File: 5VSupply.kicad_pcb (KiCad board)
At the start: 2 copper layers, 20.2 x 13 mm, 15 parts, among them J1 Conn_01x02, J2 Conn_01x02, U1 TPS560200DBVR

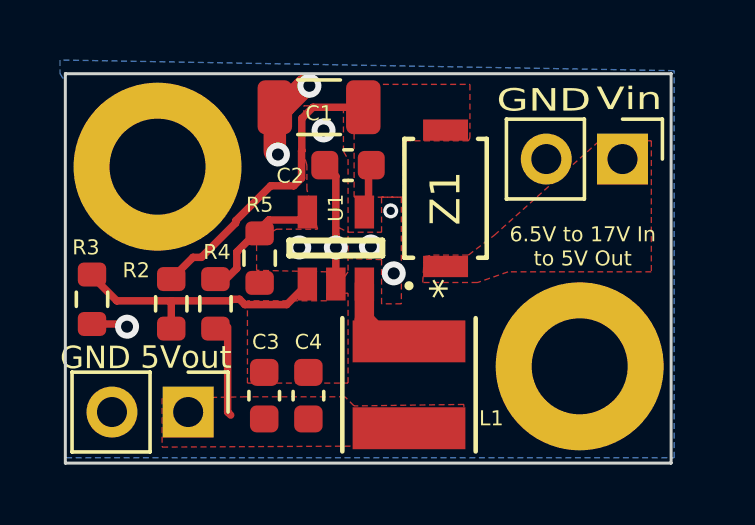
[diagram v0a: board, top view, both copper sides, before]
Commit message: PCB submitted for order
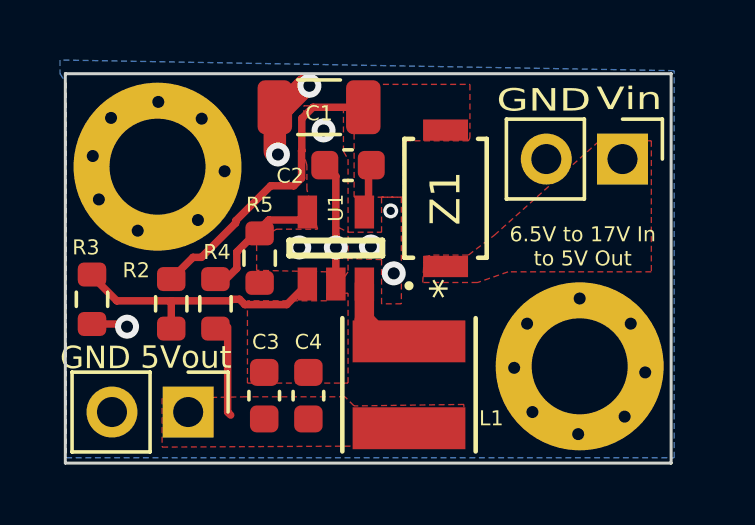
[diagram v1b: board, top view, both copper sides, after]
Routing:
- net GND: vias 9 -> 25
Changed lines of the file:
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@@
     (fp_arc (start -0.724999 1.475) (mid -0.778213 1.452901) (end -0.80074 1.399867)
       (stroke (width 0.127) (type solid)) (layer "F.Fab"))
-    (fp_arc (start 0.723714 -1.445998) (mid 0.776937 -1.423889) (end 0.799455 -1.37084)
+    (fp_arc (start 0.723714 -1.445998) (mid 0.77694 -1.423891) (end 0.799455 -1.37084)
       (stroke (width 0.127) (type solid)) (layer "F.Fab"))
-    (fp_arc (start 0.799455 1.399868) (mid 0.776925 1.452897) (end 0.723713 1.475)
+    (fp_arc (start 0.799455 1.399868) (mid 0.776922 1.452894) (end 0.723713 1.475)
       (stroke (width 0.127) (type solid)) (layer "F.Fab"))
     (pad "1" smd rect (at -1.2 -0.950001 180) (size 0.650001 1.1) (layers "F.Cu" "F.Paste" "F.Mask")
@@
   (segment (start 136.5118 80.073) (end 136.6012 80.1624) (width 0.25) (layer "F.Cu") (net 2))
   (segment (start 143.0906 74.8792) (end 143.1922 74.7776) (width 0.25) (layer "F.Cu") (net 2))
+  (via (at 149.5044 81.534) (size 0.8) (drill 0.4) (layers "F.Cu" "B.Cu") (net 2))
+  (via (at 153.8732 81.6864) (size 0.8) (drill 0.4) (layers "F.Cu" "B.Cu") (net 2))
   (via (at 136.6012 80.1624) (size 0.8) (drill 0.4) (layers "F.Cu" "B.Cu") (net 2))
+  (via (at 151.638 83.7438) (size 0.8) (drill 0.4) (layers "F.Cu" "B.Cu") (net 2))
+  (via (at 150.114 83.0072) (size 0.8) (drill 0.4) (layers "F.Cu" "B.Cu") (net 2))
+  (via (at 136.9568 76.962) (size 0.8) (drill 0.4) (layers "F.Cu" "B.Cu") (net 2))
   (via (at 145.3896 76.3016) (size 0.5) (drill 0.275) (layers "F.Cu" "B.Cu") (net 2))
   (via (at 142.679693 72.132557) (size 0.8) (drill 0.4) (layers "F.Cu" "B.Cu") (net 2))
+  (via (at 139.8524 74.9808) (size 0.8) (drill 0.4) (layers "F.Cu" "B.Cu") (net 2))
+  (via (at 139.0904 73.2282) (size 0.8) (drill 0.4) (layers "F.Cu" "B.Cu") (net 2))
+  (via (at 137.6426 72.6694) (size 0.8) (drill 0.4) (layers "F.Cu" "B.Cu") (net 2))
+  (via (at 153.3906 80.0608) (size 0.8) (drill 0.4) (layers "F.Cu" "B.Cu") (net 2))
   (via (at 142.3416 77.5208) (size 0.8) (drill 0.4) (layers "F.Cu" "B.Cu") (net 2))
   (via (at 144.7292 77.489502) (size 0.8) (drill 0.4) (layers "F.Cu" "B.Cu") (net 2))
   (via (at 141.6304 74.422) (size 0.8) (drill 0.4) (layers "F.Cu" "B.Cu") (net 2))
+  (via (at 151.6888 79.2226) (size 0.8) (drill 0.4) (layers "F.Cu" "B.Cu") (net 2))
+  (via (at 138.9634 76.6064) (size 0.8) (drill 0.4) (layers "F.Cu" "B.Cu") (net 2))
   (via (at 145.4912 78.3844) (size 0.8) (drill 0.4) (layers "F.Cu" "B.Cu") (net 2))
+  (via (at 136.0678 73.2028) (size 0.8) (drill 0.4) (layers "F.Cu" "B.Cu") (net 2))
+  (via (at 149.9362 80.0608) (size 0.8) (drill 0.4) (layers "F.Cu" "B.Cu") (net 2))
+  (via (at 135.6614 75.9206) (size 0.8) (drill 0.4) (layers "F.Cu" "B.Cu") (net 2))
+  (via (at 153.1874 83.1596) (size 0.8) (drill 0.4) (layers "F.Cu" "B.Cu") (net 2))
   (via (at 143.1515 73.62015) (size 0.8) (drill 0.4) (layers "F.Cu" "B.Cu") (net 2))
+  (via (at 135.4582 74.4728) (size 0.8) (drill 0.4) (layers "F.Cu" "B.Cu") (net 2))
   (via (at 143.5608 77.5208) (size 0.8) (drill 0.4) (layers "F.Cu" "B.Cu") (net 2))
   (segment (start 139.954 80.1746) (end 139.954 83.0072) (width 0.25) (layer "F.Cu") (net 3))
